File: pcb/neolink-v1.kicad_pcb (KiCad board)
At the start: 2 copper layers, 120 x 90 mm, 11 parts, among them J1 ESP32_2x16, J10 ANT_GSM, J2 SIM800L_1x6, J3 MAX31865_1, J4 MAX31865_2, J5 SHT35_1, J6 SHT35_2, J7 PT100_1, J8 PT100_2, J9 LiPo

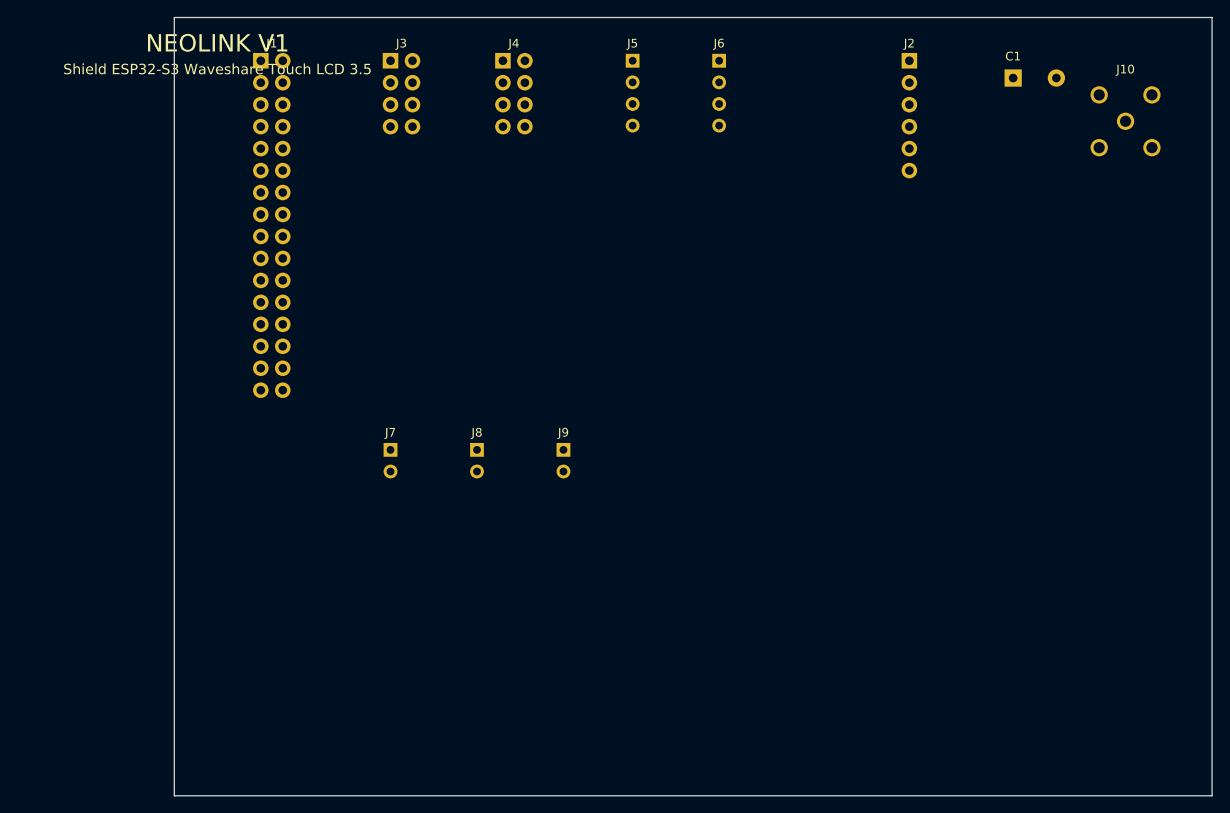
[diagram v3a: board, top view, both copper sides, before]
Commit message: Add KiCad PCB layout with complete routing and DRC pass
- Component placement: J1 ESP32 center, J2 SIM800L right (y-aligned to J1 row midpoints),
  J3/J4 MAX31865 left, J5/J6 SHT35 right, J7/J8 PT100 top-right,
  J9 LiPo bottom-left, J10 SMA bottom-right, C1 cap next to SIM800L
- Board outline: 110×80 mm
- F.Cu routing: power nets (VCC_3V3/5V/GND/BAT) at 1.0 mm, signal nets at 0.5 mm
- B.Cu: GND copper pour
- DRC: 0 shorts, 0 unconnected, 0 clearance violations (44 tracks_crossing — unavoidable single-layer)
- Pad size reduced to 1.3 mm/0.8 mm drill for routing clearance between 2.54 mm header rows
- Euclidean clearance check and trace-width-aware collision detection in gen.py router

Co-authored-by: Cursor <cursoragent@cursor.com>
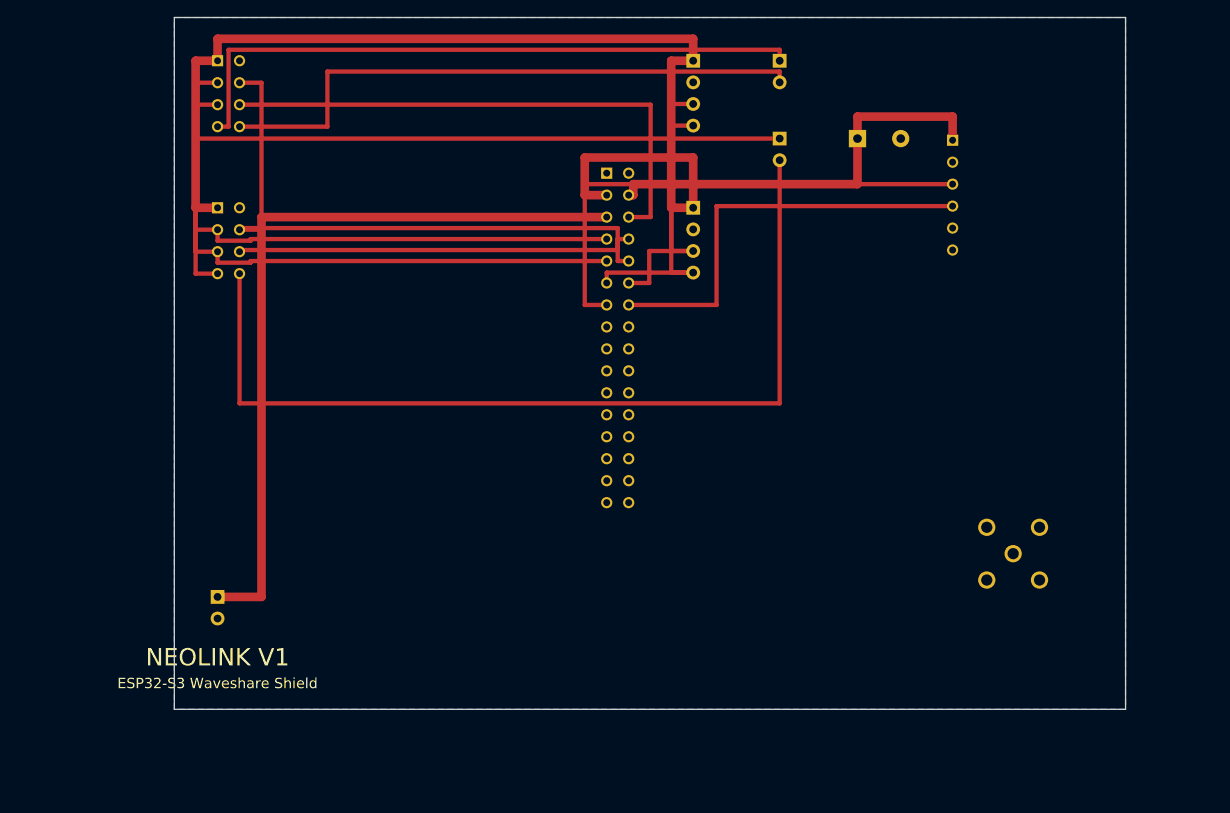
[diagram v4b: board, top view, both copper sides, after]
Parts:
- moved J7 63.6 mm to (70.0, 5.00)
- moved J10 51.7 mm to (97.0, 62.0)
- moved J8 50.2 mm to (70.0, 14.0)
- moved J9 43.5 mm to (5.00, 67.0)
- moved J1 42.1 mm to (50.0, 18.0)
- moved J4 37.1 mm to (5.00, 22.0)
- moved J3 20.0 mm to (5.00, 5.00)
- moved C1 19.3 mm to (79.0, 14.0)
- moved J6 17.3 mm to (60.0, 22.0)
- moved J2 10.5 mm to (90.0, 14.2)
- moved J5 7.00 mm to (60.0, 5.00)
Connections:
- C1 pad 1: (no net) -> ~{VCC_5V}
- C1 pad 2: (no net) -> GND
- J1 pad 1: (no net) -> GND
- J1 pad 10: (no net) -> MISO_SPI
- J1 pad 11: (no net) -> I2C_SCL
- J1 pad 12: (no net) -> I2C_SDA
- J1 pad 13: (no net) -> TXD_SIM
- J1 pad 14: (no net) -> RXD_SIM
- J1 pad 15: (no net) -> GPIO1
- J1 pad 16: (no net) -> GPIO2
- J1 pad 17: (no net) -> GPIO3
- J1 pad 18: (no net) -> GPIO4
- J1 pad 19: (no net) -> GPIO5
- J1 pad 2: (no net) -> GND
- J1 pad 20: (no net) -> GPIO6
- J1 pad 21: (no net) -> GPIO7
- J1 pad 22: (no net) -> GPIO8
- J1 pad 23: (no net) -> GPIO9
- J1 pad 24: (no net) -> GPIO10
- J1 pad 25: (no net) -> GPIO11
- J1 pad 26: (no net) -> GPIO12
- J1 pad 27: (no net) -> GPIO13
- J1 pad 28: (no net) -> GPIO14
- J1 pad 29: (no net) -> GPIO15
- J1 pad 3: (no net) -> ~{VCC_3V3}
- J1 pad 30: (no net) -> GPIO16
- J1 pad 31: (no net) -> GPIO17
- J1 pad 4: (no net) -> ~{VCC_5V}
- J1 pad 5: (no net) -> BAT
- J1 pad 6: (no net) -> CS_MAX1
- J1 pad 7: (no net) -> CLK_SPI
- J1 pad 8: (no net) -> CS_MAX2
- J1 pad 9: (no net) -> MOSI_SPI
- J10 pad 1: (no net) -> ANT_GSM
- J10 pad 2: (no net) -> GND
- J10 pad 3: (no net) -> GND
- J10 pad 4: (no net) -> GND
- J10 pad 5: (no net) -> GND
- J2 pad 1: (no net) -> ~{VCC_5V}
- J2 pad 2: (no net) -> GND
- J2 pad 3: (no net) -> TXD_SIM
- J2 pad 4: (no net) -> RXD_SIM
- J2 pad 5: (no net) -> RST_SIM
- J2 pad 6: (no net) -> PWR_SIM
- J3 pad 1: (no net) -> ~{VCC_3V3}
- J3 pad 2: (no net) -> GND
- J3 pad 3: (no net) -> CLK_SPI
- J3 pad 4: (no net) -> MISO_SPI
- J3 pad 5: (no net) -> MOSI_SPI
- J3 pad 6: (no net) -> CS_MAX1
- J3 pad 7: (no net) -> RTD1_P
- J3 pad 8: (no net) -> RTD1_N
- J4 pad 1: (no net) -> ~{VCC_3V3}
- J4 pad 2: (no net) -> GND
- J4 pad 3: (no net) -> CLK_SPI
- J4 pad 4: (no net) -> MISO_SPI
- J4 pad 5: (no net) -> MOSI_SPI
- J4 pad 6: (no net) -> CS_MAX2
- J4 pad 7: (no net) -> RTD2_P
- J4 pad 8: (no net) -> RTD2_N
- J5 pad 1: (no net) -> ~{VCC_3V3}
- J5 pad 2: (no net) -> GND
- J5 pad 3: (no net) -> I2C_SDA
- J5 pad 4: (no net) -> I2C_SCL
- J6 pad 1: (no net) -> ~{VCC_3V3}
- J6 pad 2: (no net) -> GND
- J6 pad 3: (no net) -> I2C_SDA
- J6 pad 4: (no net) -> I2C_SCL
- J7 pad 1: (no net) -> RTD1_P
- J7 pad 2: (no net) -> RTD1_N
- J8 pad 1: (no net) -> RTD2_P
- J8 pad 2: (no net) -> RTD2_N
- J9 pad 1: (no net) -> BAT
- J9 pad 2: (no net) -> GND
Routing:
- net ~{VCC_3V3}: track 0.00 -> 129.5 mm
- net RTD2_N: track 0.00 -> 105.6 mm
- net BAT: track 0.00 -> 88.9 mm
- net RTD2_P: track 0.00 -> 85.7 mm
- net RTD1_P: track 0.00 -> 75.2 mm
- net MISO_SPI: track 0.00 -> 71.1 mm
- net RTD1_N: track 0.00 -> 70.1 mm
- net CLK_SPI: track 0.00 -> 68.5 mm
- net MOSI_SPI: track 0.00 -> 68.5 mm
- net CS_MAX1: track 0.00 -> 63.1 mm
- net TXD_SIM: track 0.00 -> 59.0 mm
- net ~{VCC_5V}: track 0.00 -> 49.3 mm
- net RXD_SIM: track 0.00 -> 48.9 mm
- net CS_MAX2: track 0.00 -> 46.5 mm
- net I2C_SCL: track 0.00 -> 33.3 mm
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- added copper zone on B.Cu, net GND
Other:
- board size 120 x 90 mm -> 110 x 80 mm
- board text added: "ESP32-S3 Waveshare Shield"
- board text removed: "Shield ESP32-S3 Waveshare Touch LCD 3.5"

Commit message: PCB: 80x50mm redesign with 0 DRC electrical errors
- New placement: J1 center, J3/J4 left, J2 right, J5/J6 top-right,
  J7/J8 top-left, J9 bottom-left, J10 bottom-right, C1 next to J2
- F.Cu + B.Cu two-layer routing with 0 tracks_crossing
- Via-based routing fallback with full clearance enforcement
- Parallel track spacing checks in ch/cv closures
- GND solid zone fill on B.Cu (no starved thermal)
- Silkscreen text repositioned away from pads and board edge
- Gerbers exported: F.Cu, B.Cu, masks, silkscreen, Edge.Cuts, drill

Co-authored-by: Cursor <cursoragent@cursor.com>
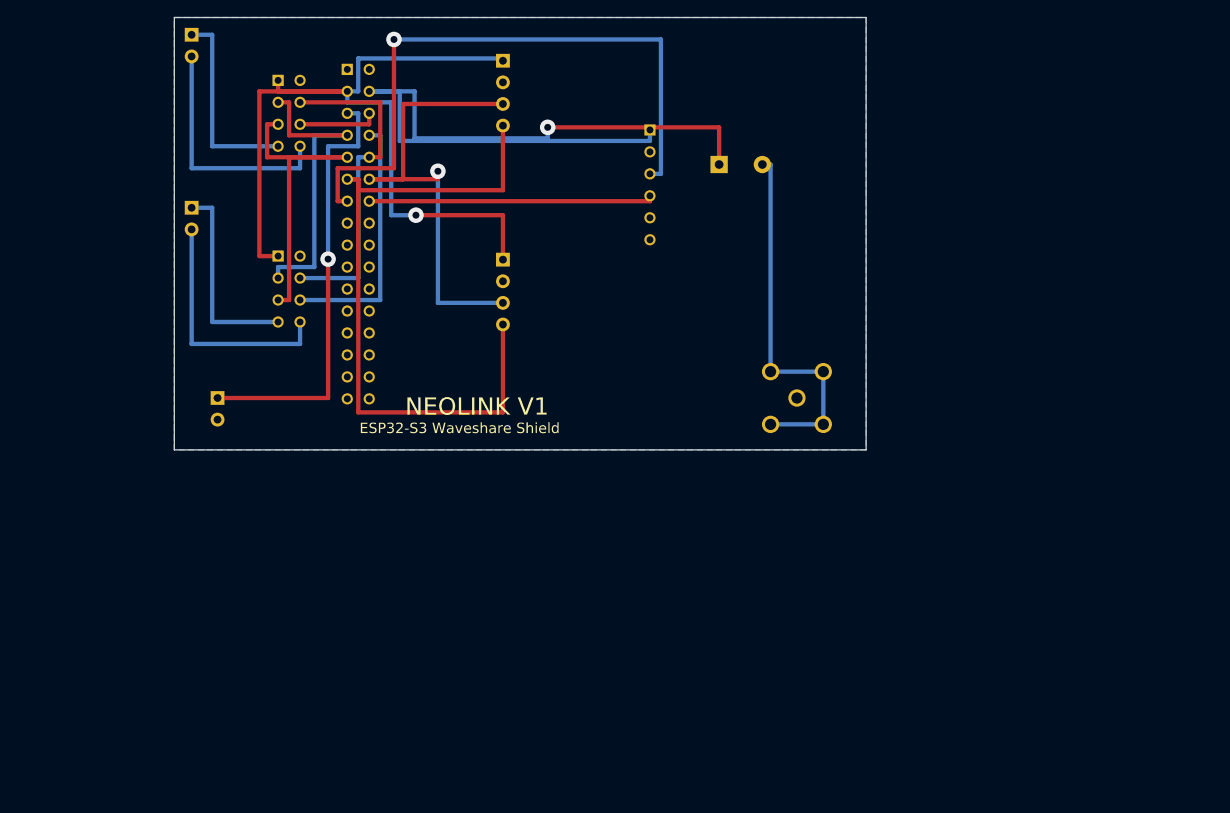
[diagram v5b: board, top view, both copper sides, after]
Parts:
- moved J8 68.5 mm to (2.00, 22.0)
- moved J7 68.1 mm to (2.00, 2.00)
- moved J2 35.0 mm to (55.0, 13.0)
- moved J1 32.3 mm to (20.0, 6.00)
- moved J10 30.8 mm to (72.0, 44.0)
- moved J9 23.0 mm to (5.00, 44.0)
- moved J6 22.8 mm to (38.0, 28.0)
- moved J5 22.0 mm to (38.0, 5.00)
- moved C1 16.3 mm to (63.0, 17.0)
- moved J4 8.96 mm to (12.0, 27.6)
- moved J3 7.36 mm to (12.0, 7.27)
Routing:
- net RTD2_N: track 105.6 -> 28.3 mm
- net RTD2_P: track 85.7 -> 23.2 mm
- net CS_MAX1: track 63.1 -> 9.27 mm
- net RTD1_P: track 75.2 -> 22.9 mm
- net I2C_SCL: track 33.3 -> 81.9 mm
- net GND: track 0.00 -> 43.2 mm
- net RTD1_N: track 70.1 -> 28.0 mm
- net ~{VCC_5V}: track 49.3 -> 90.9 mm, vias 0 -> 1
- net BAT: track 88.9 -> 50.5 mm, vias 0 -> 1
- net CLK_SPI: track 68.5 -> 36.3 mm
- net MISO_SPI: track 71.1 -> 38.9 mm
- net MOSI_SPI: track 68.5 -> 38.9 mm
- net ~{VCC_3V3}: track 129.5 -> 100.2 mm, vias 0 -> 1
- net I2C_SDA: track 33.2 -> 55.8 mm, vias 0 -> 1
- net CS_MAX2: track 46.5 -> 29.6 mm
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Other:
- board size 110 x 80 mm -> 80 x 50 mm

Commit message: PCB: complete 0-FALLBACK routing on 50×80mm portrait layout
- Fix J3_YRANGE hint bug: add x<15 guard to prevent VCC_5V getting
  spurious F.Cu hint (was blocking B.Cu corridors across the board)
- Remove J3→J4 F.Cu hint: let SPI hops choose layer freely, freeing
  F.Cu for I2C via routes
- Swap I2C_SDA/SCL in ESP32_PINS: SDA on left col (x=2.54) enables
  leftward B.Cu escape toward vias without hitting SPI pads
- Add 1.25 mm to all jog/S-bend offset candidates (_DX, _DY, C/D/E+F)
  enabling exact clearance approach to 2.50 mm pitch JST pads
- EARLY_NETS: add I2C_SDA/SCL (claim B.Cu corridors before CS_MAX2),
  add RTD1_N; remove CS_MAX2 (now routes cleanly in rest order)
- FORCE_FCU: only RTD1_N (frees middle B.Cu corridor for I2C vias)
- 0 FALLBACKs, 0 unconnected items, 0 electrical DRC violations

Co-authored-by: Cursor <cursoragent@cursor.com>
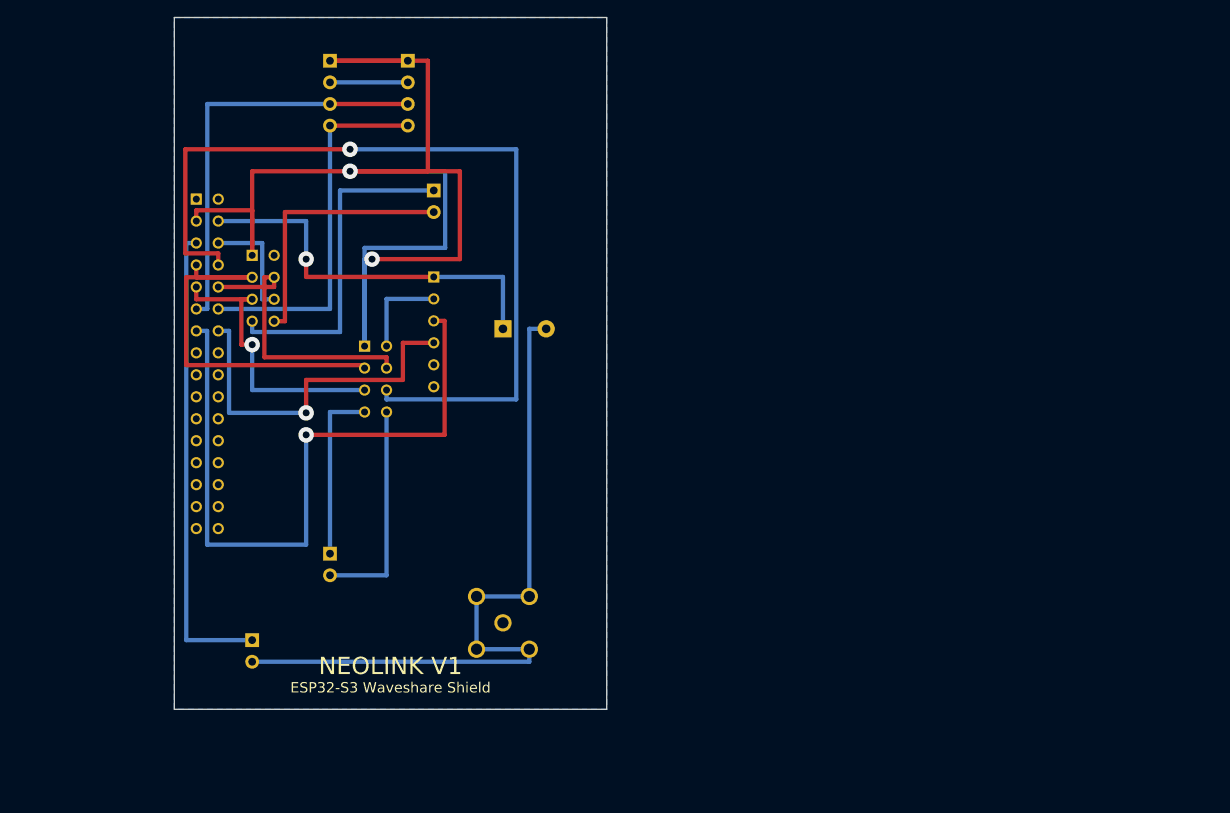
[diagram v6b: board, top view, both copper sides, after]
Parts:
- moved J8 43.1 mm to (18.0, 62.0)
- moved J10 42.8 mm to (38.0, 70.0)
- moved J7 33.3 mm to (30.0, 20.0)
- moved C1 31.4 mm to (38.0, 36.0)
- moved J2 30.2 mm to (30.0, 30.0)
- moved J9 28.3 mm to (9.00, 72.0)
- moved J6 25.5 mm to (27.0, 5.00)
- moved J1 23.0 mm to (2.54, 21.0)
- moved J3 20.5 mm to (9.00, 27.5)
- moved J5 20.0 mm to (18.0, 5.00)
- moved J4 14.4 mm to (22.0, 38.0)
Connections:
- J1 pad 11: I2C_SCL -> I2C_SDA
- J1 pad 12: I2C_SDA -> I2C_SCL
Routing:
- net CS_MAX2: track 29.6 -> 100.5 mm, vias 0 -> 1
- net GND: track 43.2 -> 104.6 mm
- net ~{VCC_3V3}: track 100.2 -> 160.5 mm, vias 1 -> 2
- net ~{VCC_5V}: track 90.9 -> 45.4 mm
- net I2C_SCL: track 81.9 -> 43.1 mm
- net RTD1_P: track 22.9 -> 38.6 mm
- net CLK_SPI: track 36.3 -> 46.6 mm
- net RXD_SIM: track 33.1 -> 42.5 mm, vias 0 -> 1
- net I2C_SDA: track 55.8 -> 48.2 mm, vias 1 -> 0
- net TXD_SIM: track 74.0 -> 80.6 mm
- net MISO_SPI: track 38.9 -> 33.3 mm
- net MOSI_SPI: track 38.9 -> 33.9 mm, vias 0 -> 1
- net BAT: track 50.5 -> 54.7 mm, vias 1 -> 0
- net CS_MAX1: track 9.27 -> 13.0 mm
- net RTD1_N: track 28.0 -> 31.1 mm
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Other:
- board size 80 x 50 mm -> 50 x 80 mm

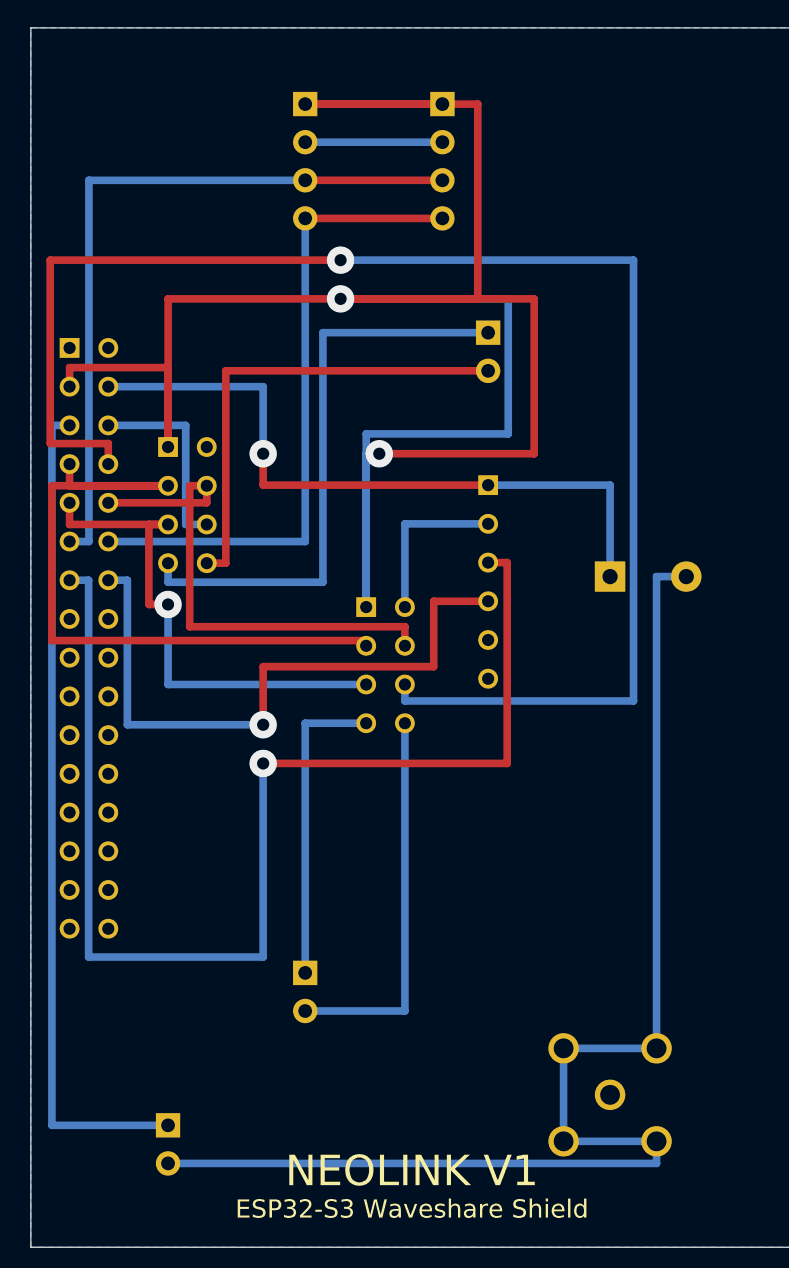
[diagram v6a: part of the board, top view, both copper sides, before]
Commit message: Add F.Silkscreen pin labels for all connectors
Each connector now has 0.8 mm silk labels for every pin:
 - J1 ESP32 2×16: auto-derived names (GND, BAT, 3V3, 5V, CLK, MOSI,
   MISO, SDA, SCL, TXD, RXD, CS1, CS2, GPIO*)
 - J2 SIM800L: VCC, GND, TXD, RXD, RST, NET
 - J3/J4 MAX31865: VIN, GND, CLK, SDO, SDI, CS, RTD+, RTD-
 - J5/J6 SHT35: VCC, GND, SDA, SCL
 - J7/J8 PT100: RTD+, RTD-
 - J9 LiPo: BAT+, BAT-
 - J10 SMA: ANT, GND

Labels generated as gr_text elements on F.SilkS.
DRC: 0 unconnected, 0 electrical errors, silk_over_copper
violations are cosmetic-only (labels adjacent to pads).
Updated Gerbers regenerated and repacked.

Co-authored-by: Cursor <cursoragent@cursor.com>
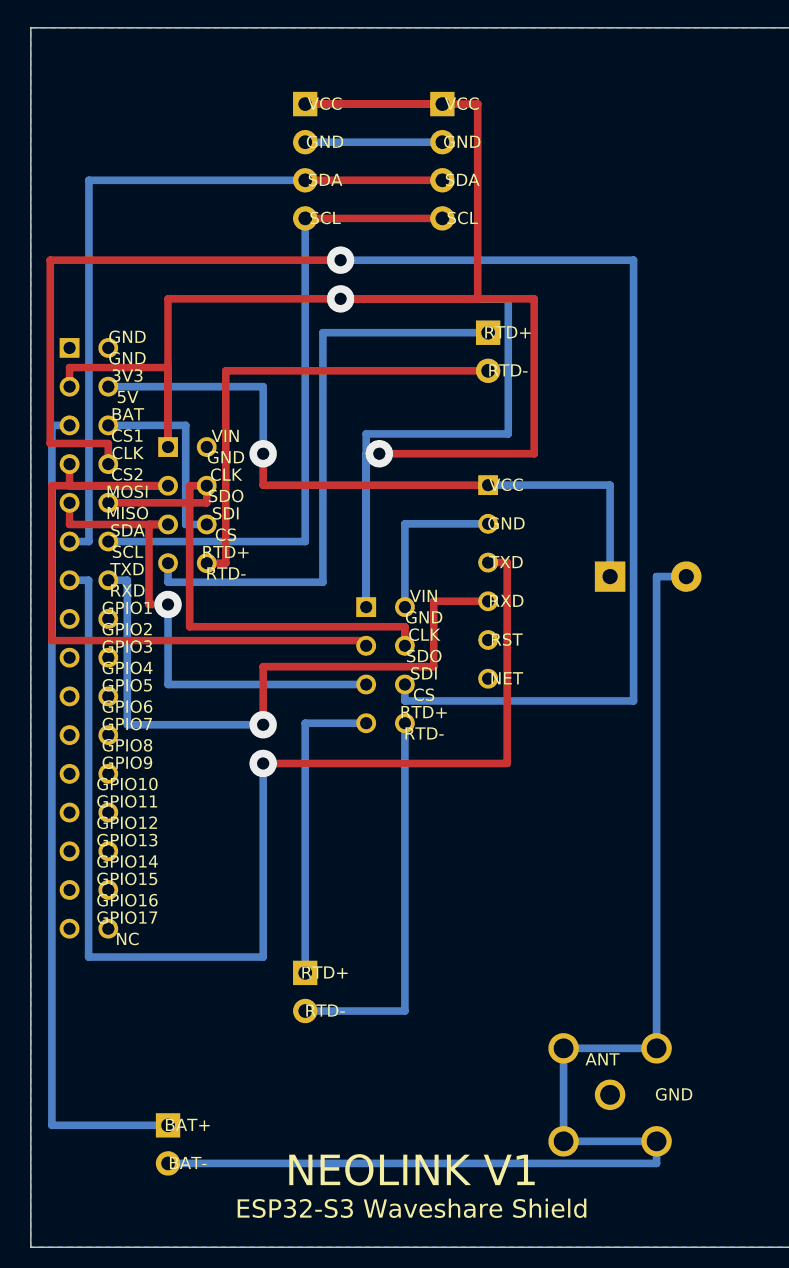
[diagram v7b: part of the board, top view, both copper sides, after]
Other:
- board text added: "3V3"
- board text added: "5V"
- board text added: "ANT"
- board text added: "BAT"
- board text added: "BAT+"
- board text added: "BAT-"
- board text added: "CLK"
- board text added: "CS"
- board text added: "CS1"
- board text added: "CS2"
- board text added: "GND"
- board text added: "GPIO1"
- board text added: "GPIO10"
- board text added: "GPIO11"
- board text added: "GPIO12"
- board text added: "GPIO13"
- board text added: "GPIO14"
- board text added: "GPIO15"
- board text added: "GPIO16"
- board text added: "GPIO17"
- board text added: "GPIO2"
- board text added: "GPIO3"
- board text added: "GPIO4"
- board text added: "GPIO5"
- board text added: "GPIO6"
- board text added: "GPIO7"
- board text added: "GPIO8"
- board text added: "GPIO9"
- board text added: "MISO"
- board text added: "MOSI"
- board text added: "NC"
- board text added: "NET"
- board text added: "RST"
- board text added: "RTD+"
- board text added: "RTD-"
- board text added: "RXD"
- board text added: "SCL"
- board text added: "SDA"
- board text added: "SDI"
- board text added: "SDO"
- board text added: "TXD"
- board text added: "VCC"
- board text added: "VIN"
